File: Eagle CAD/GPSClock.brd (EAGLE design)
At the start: 100 x 80 mm, 39 parts, among them IC3 LM1117, J1 AMP FCI 10103594-0001LF, J2 ISP, J3 POWER_JACKSUPER_BOMB_DIGITY, J4 BM06B-SRSS-TB, Q1 1A/60V/500mΩ, U1 CH340C, U3 AP2112-3.3V, U4 ATMEGA328P_TQFP, Y1 16MHz

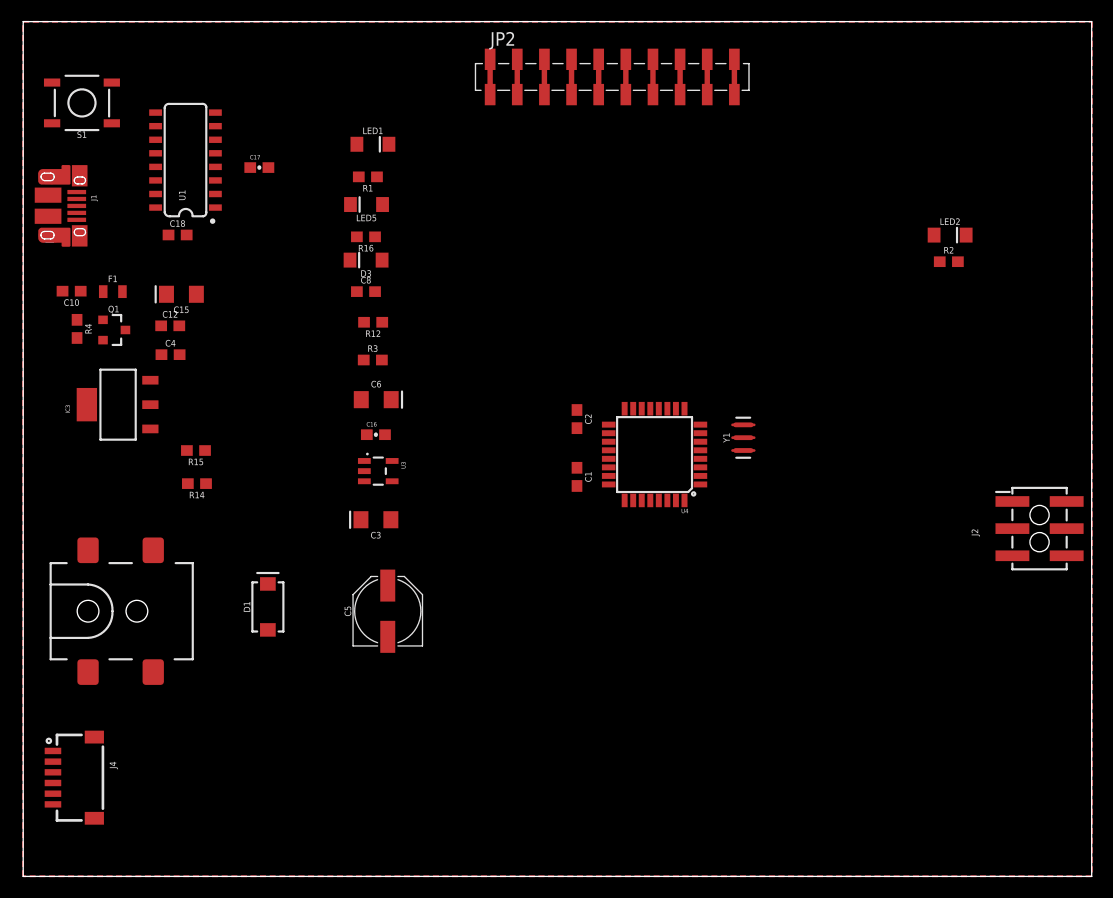
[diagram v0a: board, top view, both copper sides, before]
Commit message: updated GPS connection, auto routing for starting point
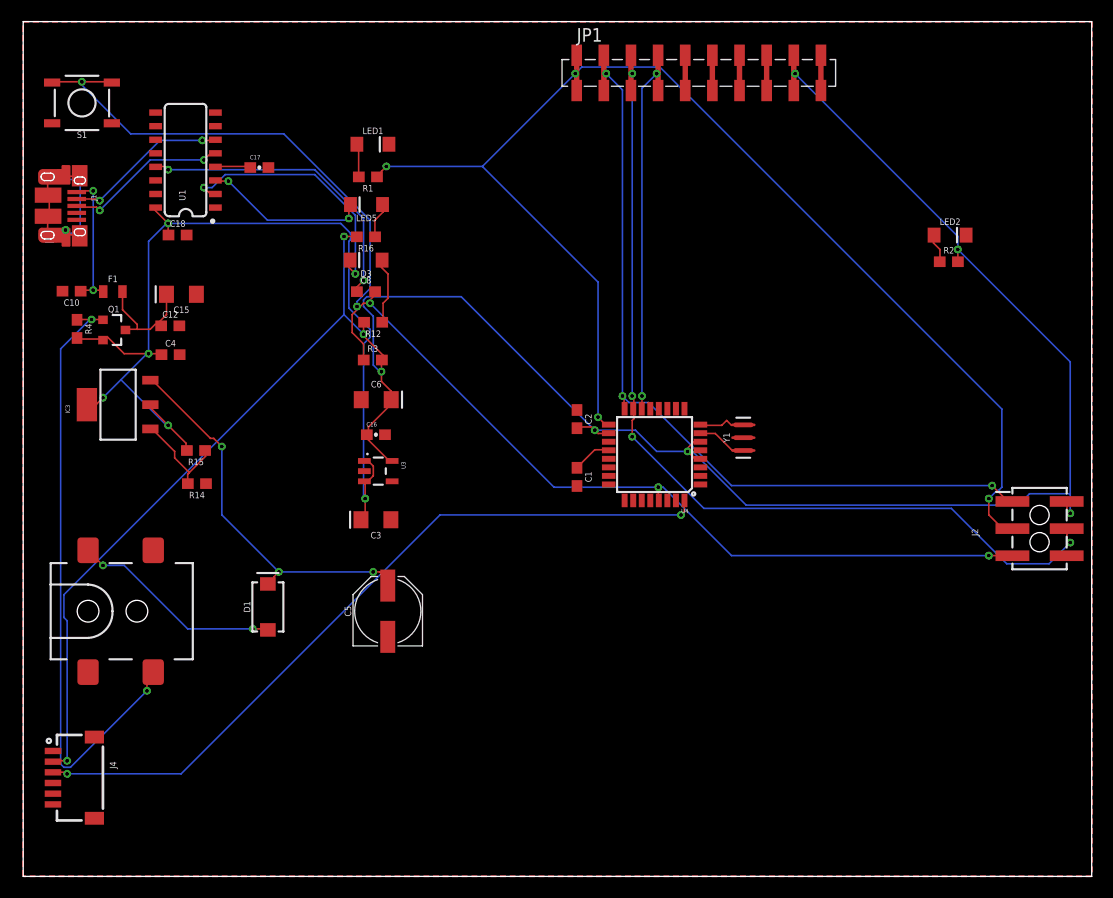
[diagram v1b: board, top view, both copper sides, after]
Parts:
- removed JP2: M10SMD_COMBO, SparkFun-Connectors:1X10_SMD_COMBINED
- added JP1: M10SMD_COMBO, SparkFun-Connectors:1X10_SMD_COMBINED
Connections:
- removed net IO8: JP2.10A, JP2.10B, U4.12
- removed net IO9: JP2.9A, JP2.9B, U4.13
- net GND: now also JP1.10A, JP1.10B; no longer JP2.1A, JP2.1B
- net MISO: now also JP1.2A, JP1.2B; no longer JP2.6A, JP2.6B
- net MOSI: now also JP1.3A, JP1.3B; no longer JP2.7A, JP2.7B
- net SCK: now also JP1.1A, JP1.1B; no longer JP2.5A, JP2.5B
- net SS: now also JP1.4A, JP1.4B; no longer JP2.8A, JP2.8B
- net VCC: now also JP1.9A, JP1.9B; no longer JP2.2A, JP2.2B
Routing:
- net VCC: track 0.00 -> 229.8 mm, vias 0 -> 9
- net RESET: track 0.00 -> 126.5 mm, vias 0 -> 5
- net SCK: track 0.00 -> 123.7 mm, vias 0 -> 4
- net 5V: track 0.00 -> 95.5 mm, vias 0 -> 5
- net MOSI: track 0.00 -> 87.5 mm, vias 0 -> 4
- net MISO: track 0.00 -> 77.8 mm, vias 0 -> 3
- net N$7: track 0.00 -> 70.4 mm, vias 0 -> 2
- net INSERT: track 0.00 -> 58.5 mm, vias 0 -> 2
- net SS: track 0.00 -> 37.0 mm, vias 0 -> 2
- net VIN: track 0.00 -> 35.8 mm, vias 0 -> 3
- net !DTR: track 0.00 -> 28.6 mm, vias 0 -> 2
- net RX-I: track 0.00 -> 24.7 mm, vias 0 -> 2
- net SHLD: track 0.00 -> 23.3 mm, vias 0 -> 1
- net PWRIN: track 0.00 -> 19.9 mm, vias 0 -> 2
- net TX-O: track 0.00 -> 15.5 mm, vias 0 -> 2
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
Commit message: Add files via upload
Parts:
- added JP2, JP3, JP4, JP5: JUMPER-SMT_2_NC_TRACE_NO-SILK, SparkFun-Jumpers:SMT-JUMPER_2_NC_TRACE_NO-SILK
- added R7: 1M, SparkFun-Resistors:0603
- added R8: 1k, SparkFun-Resistors:0603
- added TP1: TP-063, keystone:TP-063
- added U2: LIGHT_SENSORALS, SparkFun-Sensors:ALS-PT19
- added U5: 1571984-1, TE 1571984-1:SWITCH_1571984-1
- moved J2 61.1 mm to (34.8, 23.1), turned to 90 degrees
- moved J4 53.1 mm to (32.8, 56.0)
- moved LED2 49.6 mm to (38.6, 48.0)
- moved R2 49.4 mm to (38.6, 45.8)
- moved JP1 35.8 mm to (17.0, 66.7)
- moved C6 33.3 mm to (21.4, 13.4)
- moved C16 33.2 mm to (21.5, 10.2), turned to 180 degrees
- moved U3 33.0 mm to (21.4, 7.14)
- moved C3 32.2 mm to (21.4, 3.32)
- moved Y1 24.5 mm to (43.0, 41.6)
- moved U4 23.7 mm to (35.4, 39.2)
- moved C5 23.6 mm to (11.1, 19.5), turned to 180 degrees
- moved C1 23.3 mm to (28.6, 38.8)
- moved C2 23.2 mm to (28.6, 42.1)
- moved LED1 23.2 mm to (20.6, 48.8)
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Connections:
- net N$7 renamed GPS_RX
- new net AMBIENT: R7.1, U2.C, U4.1
- new net DTS: R8.1, U4.2, U5.5
- new net N$10: JP1.9A, JP1.9B, JP4.1
- new net N$11: J4.2, JP5.1
- new net N$7: C16.1, C6.+, JP3.1, U3.5
- new net N$8: JP2.1, U3.1, U3.3
- net 5V: now also JP2.2; no longer U3.1, U3.3
- net GND: now also TP1.1, U2.E, U5.1, U5.3, U5.6
- net RX-I: now also U4.30
- net TX-O: now also U4.31
- net VCC: now also JP3.2, JP5.2, R7.2, R8.2; no longer C16.1, C6.+, J4.2, JP1.9A, JP1.9B, U3.5
- net VIN: now also JP4.2
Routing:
- net VCC: track 229.8 -> 103.3 mm, vias 9 -> 7
- net N$10: track 0.00 -> 69.4 mm, vias 0 -> 2
- net INSERT: track 58.5 -> 2.25 mm, vias 2 -> 0
- net SCK: track 123.7 -> 68.6 mm, vias 4 -> 2
- net DTS: track 0.00 -> 48.2 mm
- net RESET: track 126.5 -> 79.7 mm, vias 5 -> 4
- net AMBIENT: track 0.00 -> 46.5 mm, vias 0 -> 2
- net MOSI: track 87.5 -> 56.1 mm, vias 4 -> 2
- net GPS_RX: track 70.4 -> 40.3 mm
- net TX-O: track 15.5 -> 45.3 mm
- net RX-I: track 24.7 -> 48.1 mm
- net SHLD: track 23.3 -> 0.00 mm, vias 1 -> 0
- net 5V: track 95.5 -> 76.2 mm, vias 5 -> 2
- net MISO: track 77.8 -> 63.0 mm, vias 3 -> 2
- net N$11: track 0.00 -> 13.7 mm, vias 0 -> 2
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- removed copper zone on layer 1, net GND
- removed copper zone on layer 16, net GND
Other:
- board size 100 x 80 mm -> 59.4 x 70 mm
- board text added: "Team 9: GPS Enabled Clock ECE 411 Fall 2019 Cheng, Jemmett, Jia & Liu"

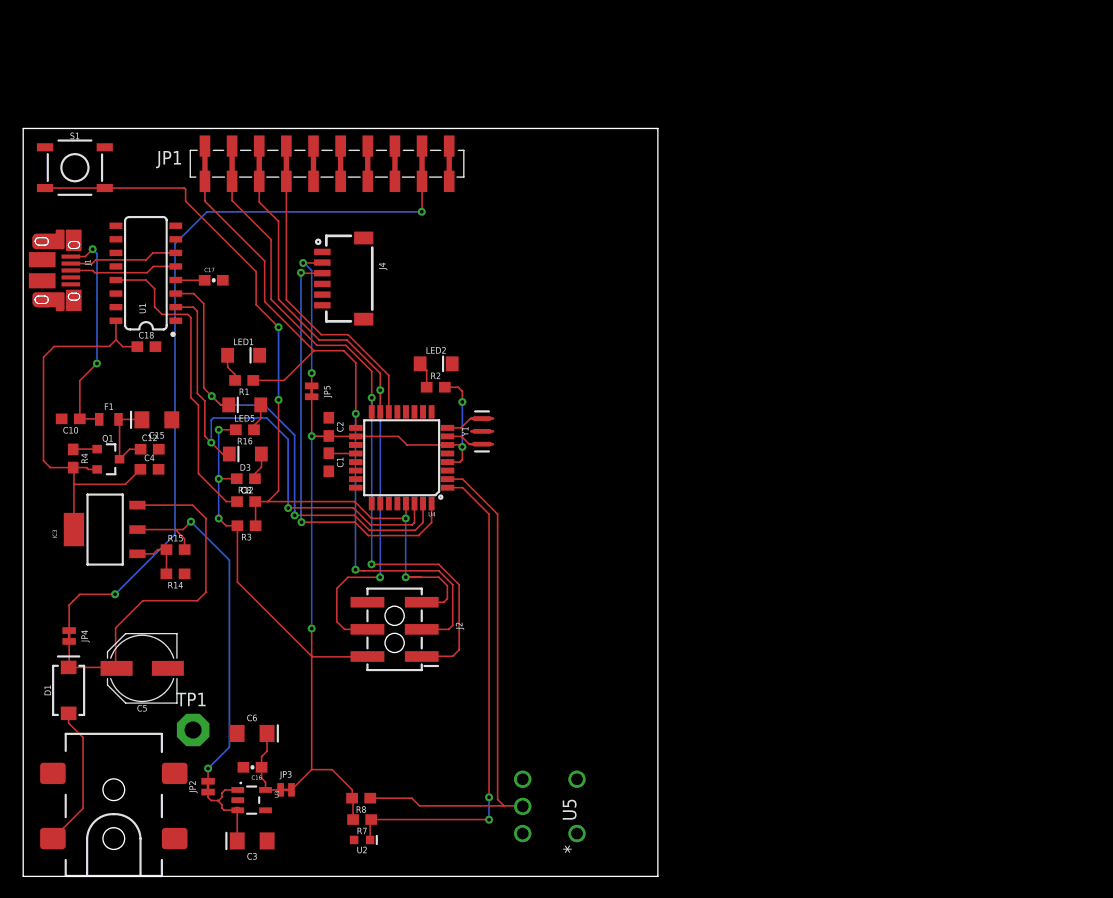
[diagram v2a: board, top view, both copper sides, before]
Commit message: Completed OSH Park's DRC
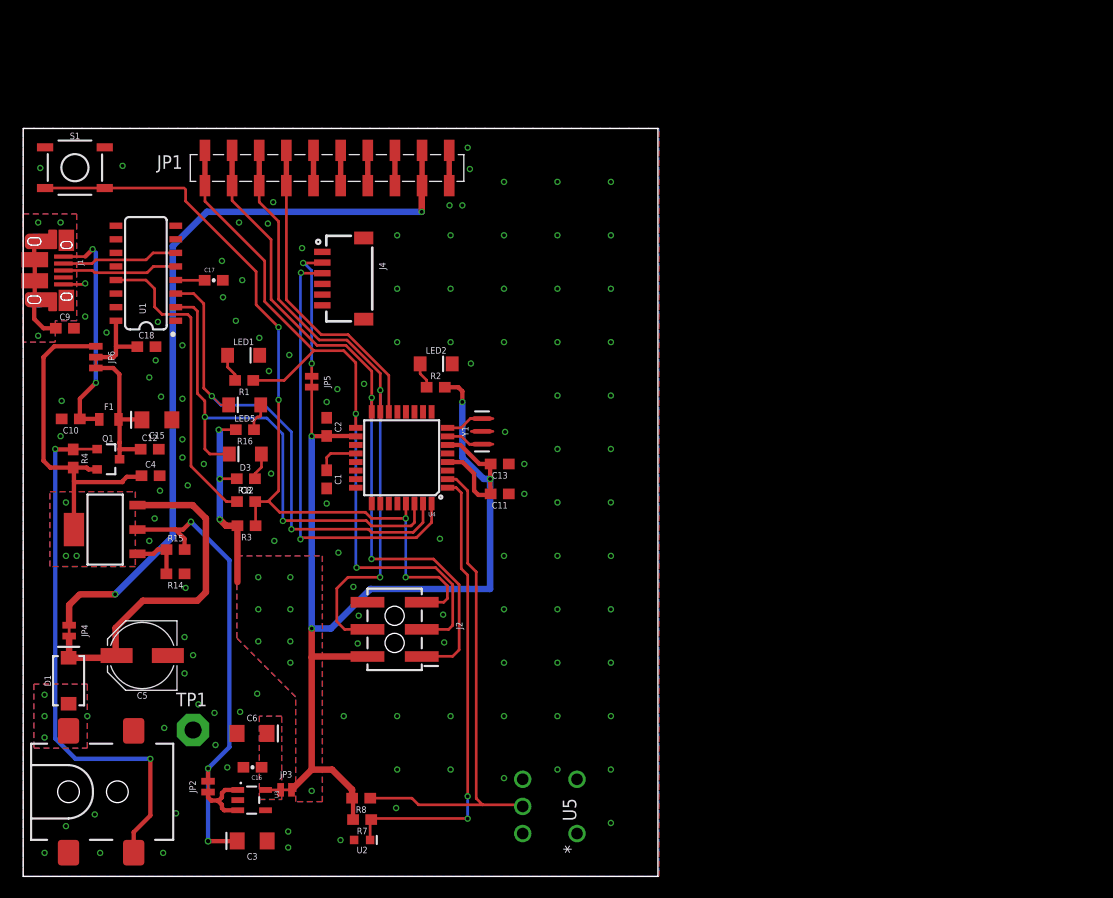
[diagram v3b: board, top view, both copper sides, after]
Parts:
- added C11, C13, C9: 0.1uF, SparkFun-Capacitors:0603
- added JP6: JUMPER-SMT_3_1-NC_TRACE_NO-SILK, SparkFun-Jumpers:SMT-JUMPER_3_1-NC_TRACE_NO-SILK
- moved J3 6.10 mm to (4.24, 7.92), turned to 0 degrees
- moved C1 1.61 mm to (28.4, 37.2)
- moved C5 1.20 mm to (11.1, 20.7)
- moved D1 0.90 mm to (4.25, 18.3)
- moved JP5 0.90 mm to (27.0, 46.3)
- moved J1 0.70 mm to (2.43, 56.7)
- moved C4 0.61 mm to (11.9, 37.5)
- moved JP4 0.50 mm to (4.30, 23.0)
- moved JP1 0.40 mm to (17.0, 66.3)
- moved C2 0.20 mm to (28.4, 42.1)
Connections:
- removed net VCC: C2.2, J2.2, JP3.2, JP5.2, R12.2, R16.2, R2.2, R3.2, R7.2, R8.2, U4.18, U4.4, U4.6
- new net 3.3V: C11.2, C13.2, C2.2, J2.2, JP3.2, JP5.2, R12.2, R16.2, R2.2, R3.2, R7.2, R8.2, U4.18, U4.4, U4.6
- new net N$12: C18.1, JP6.2, U1.16
- net 5V: now also JP6.1; no longer C18.1, U1.16
- net GND: now also C11.1, C13.1, C9.2
- net SHLD: now also C9.1
- net USBVCC: now also JP6.3
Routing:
- net 3.3V: track 0.00 -> 127.9 mm, vias 0 -> 15
- net VCC: track 103.3 -> 0.00 mm, vias 7 -> 0
- net INSERT: track 2.25 -> 50.2 mm, vias 0 -> 2
- net PWRIN: track 13.4 -> 0.00 mm, vias 0 -> 4
- net SHLD: track 0.00 -> 9.69 mm, vias 0 -> 3
- net N$12: track 0.00 -> 7.19 mm
- net USBVCC: track 8.30 -> 14.6 mm
- net N$7: track 6.71 -> 1.42 mm
- net AMBIENT: track 46.5 -> 43.3 mm
- net SS: track 27.0 -> 29.9 mm
- net MOSI: track 56.1 -> 59.0 mm
- net MISO: track 63.0 -> 65.6 mm
- net SCK: track 68.6 -> 71.2 mm
- net N$10: track 69.4 -> 71.8 mm
- net GND: track 0.00 -> 2.08 mm, vias 0 -> 117
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- added copper zone on layer 1, net 3.3V
- added copper zone on layer 16, net 3.3V
- added copper zone on layer 1, net 5V
- added copper zone on layer 16, net 5V
- added copper zone on layer 1, net GND
- added copper zone on layer 16, net GND
- added copper zone on layer 1, net N$7
- added copper zone on layer 16, net N$7
- added copper zone on layer 1, net PWRIN
- added copper zone on layer 16, net PWRIN
- added copper zone on layer 1, net SHLD
- added copper zone on layer 16, net SHLD

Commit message: Fixed board size
Fixed board size and power connector location to allow for LCD connection
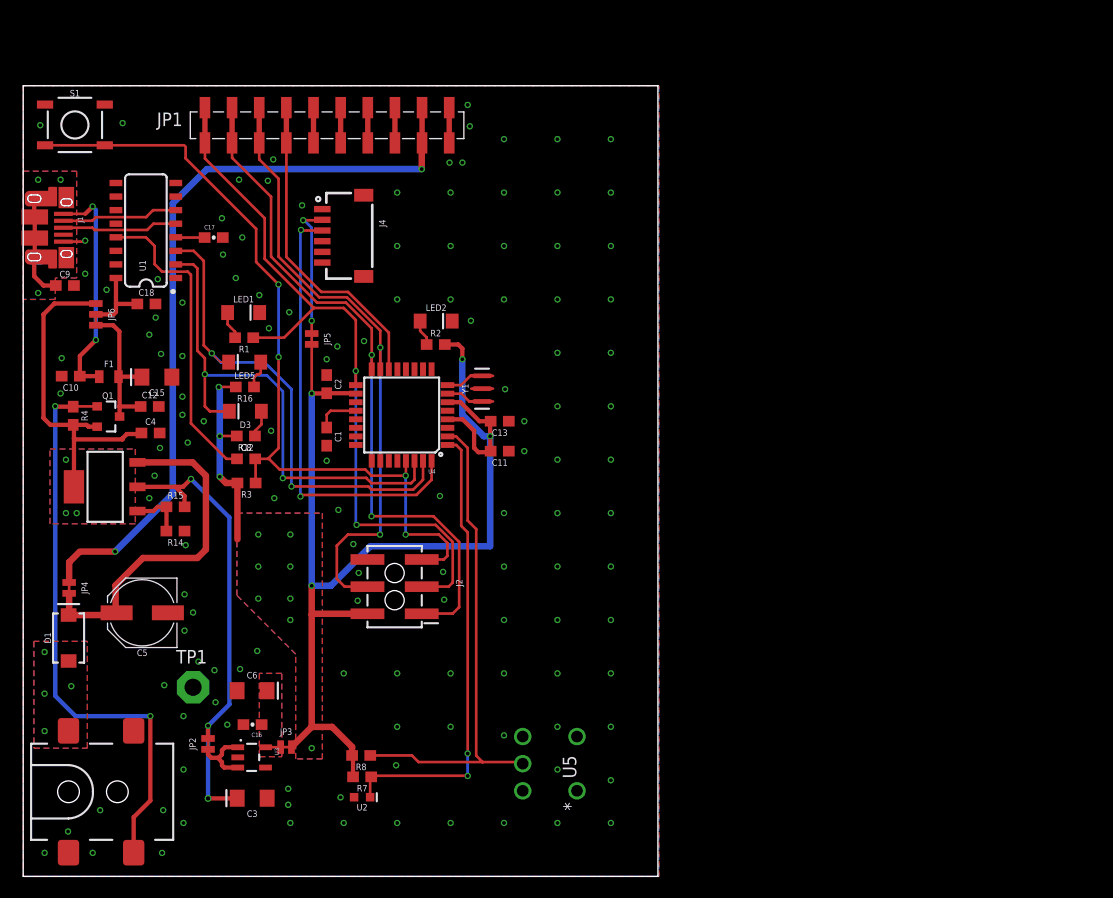
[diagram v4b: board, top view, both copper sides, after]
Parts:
- moved R15 4.00 mm to (14.3, 34.6)
- moved U3 4.00 mm to (21.4, 11.1)
- moved C1 4.00 mm to (28.4, 41.2)
- moved C10 4.00 mm to (4.45, 46.8)
- moved C11 4.00 mm to (44.6, 39.8)
- moved C12 4.00 mm to (11.8, 44.0)
- moved C13 4.00 mm to (44.6, 42.6)
- moved C15 4.00 mm to (12.5, 46.7)
- moved C16 4.00 mm to (21.5, 14.2)
- moved C17 4.00 mm to (17.8, 59.8)
- moved C18 4.00 mm to (11.5, 53.6)
- moved C2 4.00 mm to (28.4, 46.1)
- moved C3 4.00 mm to (21.4, 7.32)
- moved C4 4.00 mm to (11.9, 41.5)
- moved C5 4.00 mm to (11.1, 24.7)
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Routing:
- net INSERT: track 50.2 -> 54.2 mm
- net GND: vias 117 -> 127
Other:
- board size 59.4 x 70 mm -> 59.4 x 74 mm
